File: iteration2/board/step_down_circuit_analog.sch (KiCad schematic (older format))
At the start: 4 parts

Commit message: Redo netlist
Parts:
- C5: renamed from C?; footprint ~ -> Capacitors_SMD:C_0805_HandSoldering
- D4: renamed from D?; footprint ~ -> Diodes_SMD:D_0805
- R10, R11: renamed from R?; footprint ~ -> Resistors_SMD:R_0805_HandSoldering
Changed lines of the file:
@@
 $EndDescr
 $Comp
-L R R?
+L R R10
 U 1 1 59F280F5
 P 5200 4150
-F 0 "R?" V 5280 4150 40  0000 C CNN
+F 0 "R10" V 5280 4150 40  0000 C CNN
 F 1 "10K" V 5207 4151 40  0000 C CNN
-F 2 "~" V 5130 4150 30  0000 C CNN
+F 2 "Resistors_SMD:R_0805_HandSoldering" V 5130 4150 30  0000 C CNN
 F 3 "~" H 5200 4150 30  0000 C CNN
 	1    5200 4150
@@
 $EndComp
 $Comp
-L BAV99 D?
+L BAV99 D4
 U 1 1 59F280FC
 P 5550 4200
-F 0 "D?" H 5650 4150 40  0000 C CNN
+F 0 "D4" H 5650 4150 40  0000 C CNN
 F 1 "BAV99" H 5650 4250 40  0000 C CNN
-F 2 "~" V 5600 4150 60  0000 C CNN
+F 2 "Diodes_SMD:D_0805" V 5600 4150 60  0000 C CNN
 F 3 "~" V 5600 4150 60  0000 C CNN
 	1    5550 4200
@@
 $EndComp
 $Comp
-L R R?
+L R R11
 U 1 1 59F28103
 P 5900 4400
-F 0 "R?" V 5980 4400 40  0000 C CNN
+F 0 "R11" V 5980 4400 40  0000 C CNN
 F 1 "1M" V 5907 4401 40  0000 C CNN
-F 2 "~" V 5830 4400 30  0000 C CNN
+F 2 "Resistors_SMD:R_0805_HandSoldering" V 5830 4400 30  0000 C CNN
 F 3 "~" H 5900 4400 30  0000 C CNN
 	1    5900 4400
@@
 $EndComp
 $Comp
-L GND #PWR?
+L GND #PWR16
 U 1 1 59F2810A
 P 5550 4350
-F 0 "#PWR?" H 5550 4350 30  0001 C CNN
+F 0 "#PWR16" H 5550 4350 30  0001 C CNN
 F 1 "GND" H 5550 4280 30  0001 C CNN
 F 2 "" H 5550 4350 60  0000 C CNN
@@
 $EndComp
 $Comp
-L GND #PWR?
+L GND #PWR17
 U 1 1 59F28110
 P 5900 4650
-F 0 "#PWR?" H 5900 4650 30  0001 C CNN
+F 0 "#PWR17" H 5900 4650 30  0001 C CNN
 F 1 "GND" H 5900 4580 30  0001 C CNN
 F 2 "" H 5900 4650 60  0000 C CNN
@@
 $EndComp
 $Comp
-L C C?
+L C C5
 U 1 1 59F28116
 P 6100 4350
-F 0 "C?" H 6100 4450 40  0000 L CNN
+F 0 "C5" H 6100 4450 40  0000 L CNN
 F 1 "100nF" H 6106 4265 40  0000 L CNN
-F 2 "~" H 6138 4200 30  0000 C CNN
+F 2 "Capacitors_SMD:C_0805_HandSoldering" H 6138 4200 30  0000 C CNN
 F 3 "~" H 6100 4350 60  0000 C CNN
 	1    6100 4350
@@
 	5800 4600 5800 4150
 Wire Wire Line
-	5800 4150 5900 4150
-Wire Wire Line
-	5900 4150 6100 4150
+	5800 4150 6100 4150
 Connection ~ 5900 4150
 $Comp
-L GND #PWR?
+L GND #PWR18
 U 1 1 59F28122
 P 6100 4550
-F 0 "#PWR?" H 6100 4550 30  0001 C CNN
+F 0 "#PWR18" H 6100 4550 30  0001 C CNN
 F 1 "GND" H 6100 4480 30  0001 C CNN
 F 2 "" H 6100 4550 60  0000 C CNN

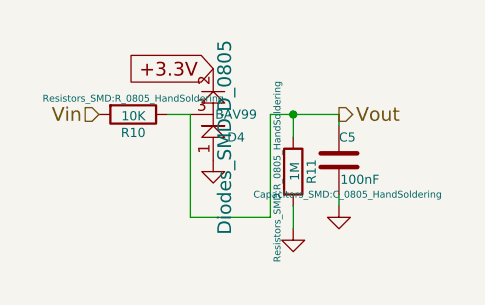
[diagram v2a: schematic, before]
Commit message: Redid some components to fit footprint
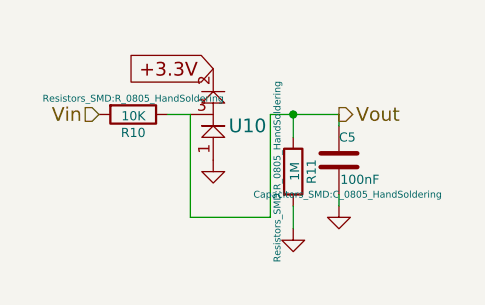
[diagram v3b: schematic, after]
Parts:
- removed D4: BAV99, Diodes_SMD:D_0805, symbol BAV99
- added U10: BAV99, TO_SOT_Packages_SMD:SOT-23, symbol BAV99
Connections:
- net +3.3V: now also U10.2
- net GND: now also U10.1
- net Vout: now also U10.3
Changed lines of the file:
@@
-$EndComp
-$Comp
-L BAV99 D4
-U 1 1 59F280FC
-P 5550 4200
-F 0 "D4" H 5650 4150 40  0000 C CNN
-F 1 "BAV99" H 5650 4250 40  0000 C CNN
-F 2 "Diodes_SMD:D_0805" V 5600 4150 60  0000 C CNN
-F 3 "~" V 5600 4150 60  0000 C CNN
-	1    5550 4200
-	1    0    0    -1
 $EndComp
 $Comp
@@
 Wire Wire Line
 	6100 4150 6100 4200
+$Comp
+L BAV99 U10
+U 1 1 59F29DD7
+P 5550 4200
+F 0 "U10" H 5700 4200 60  0000 C CNN
+F 1 "BAV99" H 5800 4300 60  0001 C CNN
+F 2 "TO_SOT_Packages_SMD:SOT-23" H 5550 4200 60  0001 C CNN
+F 3 "" H 5550 4200 60  0001 C CNN
+	1    5550 4200
+	1    0    0    -1
+$EndComp
 $EndSCHEMATC

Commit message: partially resolved merge issues and added script for automatic merging
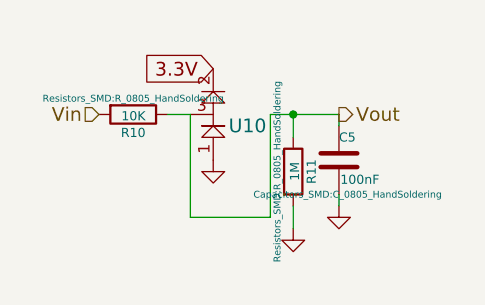
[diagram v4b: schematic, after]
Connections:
- net +3.3V renamed 3.3V
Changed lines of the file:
@@
 $EndComp
 $Comp
-L GND #PWR016
+L GND #PWR16
 U 1 1 59F2810A
 P 5550 4350
-F 0 "#PWR016" H 5550 4350 30  0001 C CNN
+F 0 "#PWR16" H 5550 4350 30  0001 C CNN
 F 1 "GND" H 5550 4280 30  0001 C CNN
 F 2 "" H 5550 4350 60  0000 C CNN
@@
 $EndComp
 $Comp
-L GND #PWR017
+L GND #PWR17
 U 1 1 59F28110
 P 5900 4650
-F 0 "#PWR017" H 5900 4650 30  0001 C CNN
+F 0 "#PWR17" H 5900 4650 30  0001 C CNN
 F 1 "GND" H 5900 4580 30  0001 C CNN
 F 2 "" H 5900 4650 60  0000 C CNN
@@
 Connection ~ 5900 4150
 $Comp
-L GND #PWR018
+L GND #PWR18
 U 1 1 59F28122
 P 6100 4550
-F 0 "#PWR018" H 6100 4550 30  0001 C CNN
+F 0 "#PWR18" H 6100 4550 30  0001 C CNN
 F 1 "GND" H 6100 4480 30  0001 C CNN
 F 2 "" H 6100 4550 60  0000 C CNN
@@
 $EndComp
 Text GLabel 5550 3950 0    60   Input ~ 0
-+3.3V
+3.3V
 Wire Wire Line
 	5900 4250 5900 4150
